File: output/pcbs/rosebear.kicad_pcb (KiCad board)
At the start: 2 copper layers, 135.3 x 105.1 mm, 43 parts

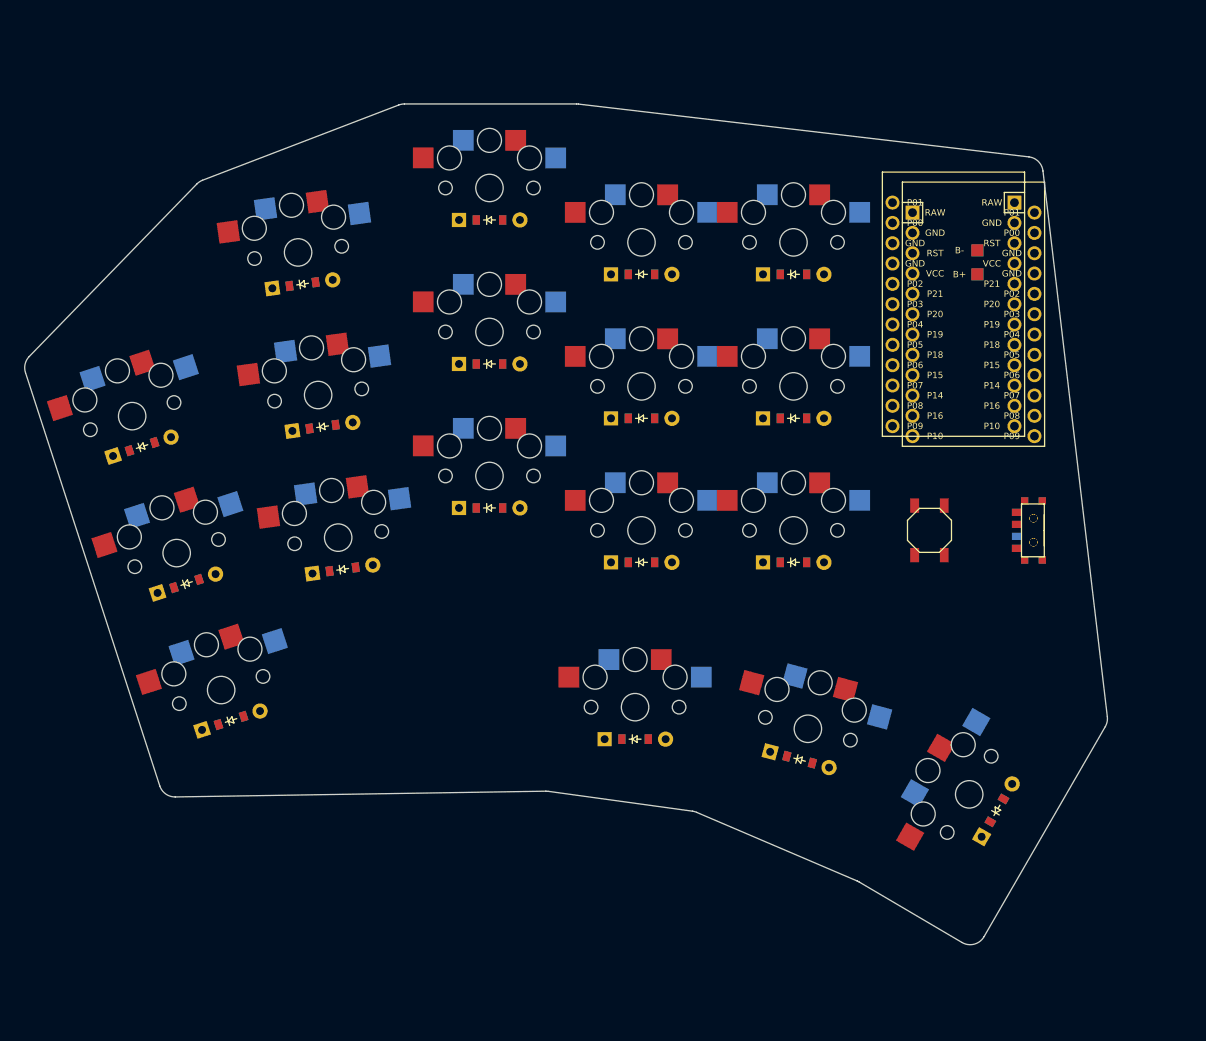
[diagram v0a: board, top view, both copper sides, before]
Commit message: inset board edge a bit
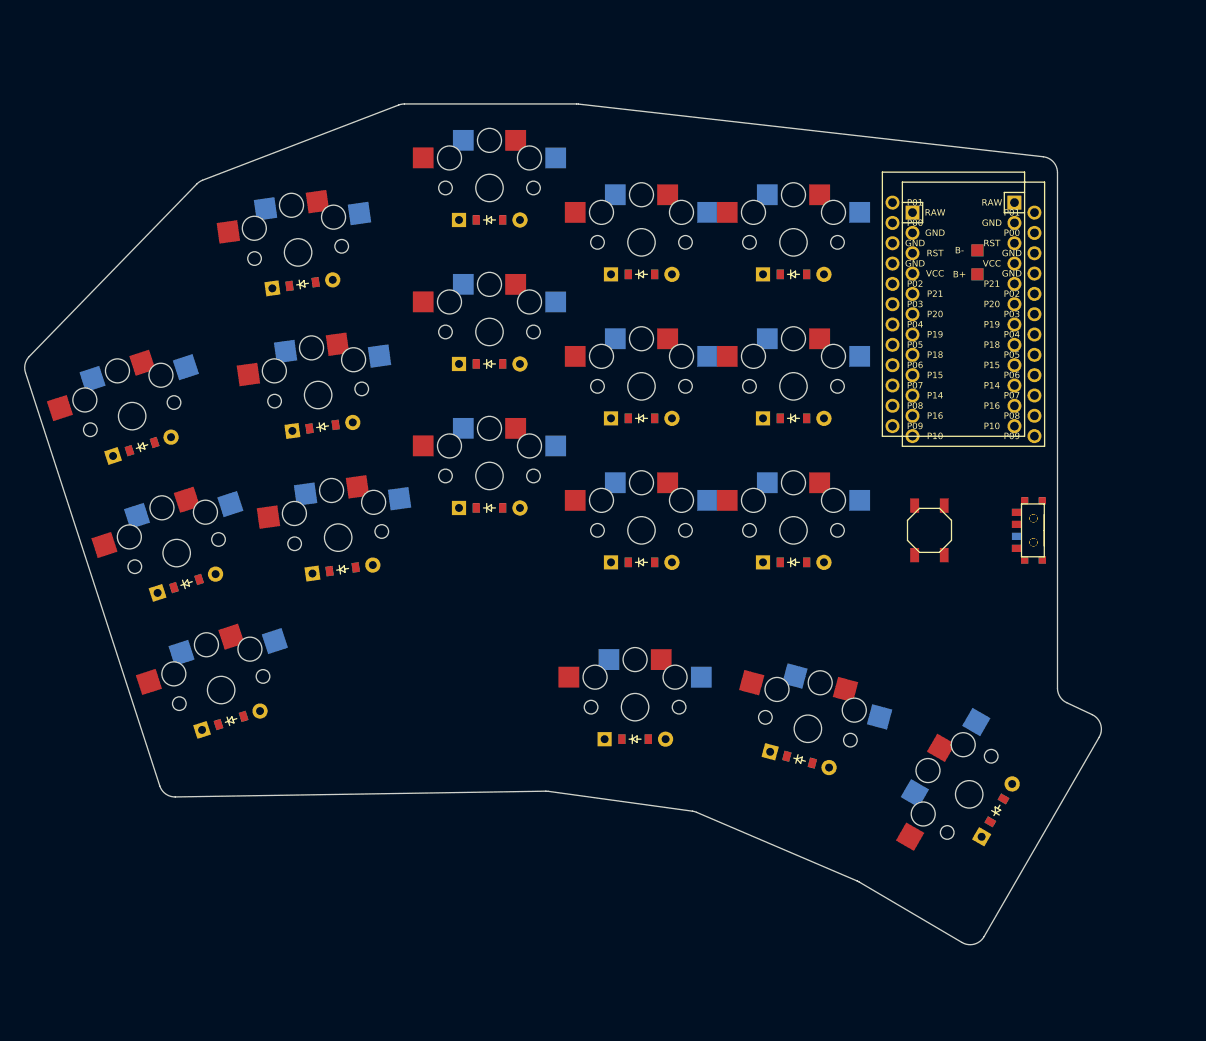
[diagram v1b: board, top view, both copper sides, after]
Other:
- board size 135.3 x 105.1 mm -> 134.6 x 105.1 mm
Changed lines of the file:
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@@
 (gr_line (start 26.00924211801839 58.31019527101077) (end 46.956701761727736 36.74665385238504) (angle 90) (layer Edge.Cuts) (width 0.15))
 (gr_line (start 47.675304323093606 36.27276563583152) (end 72.19402026968349 26.872666933425457) (angle 90) (layer Edge.Cuts) (width 0.15))
-(gr_line (start 72.90997585686867 26.740127099999995) (end 94.42288855882353 26.740127099999995) (angle 90) (layer Edge.Cuts) (width 0.15))
-(gr_line (start 94.65577615882353 26.753732499999998) (end 150.9713108649408 33.35624346554478) (angle 90) (layer Edge.Cuts) (width 0.15))
-(gr_line (start 152.72466176356932 35.10842305391452) (end 160.77044002192582 103.33990513293065) (angle 90) (layer Edge.Cuts) (width 0.15))
-(gr_line (start 160.5162523232973 104.57412014456105) (end 145.35622983220486 130.83204941203354) (angle 90) (layer Edge.Cuts) (width 0.15))
+(gr_line (start 72.90997585686867 26.740127099999995) (end 94.42675824117646 26.740127099999995) (angle 90) (layer Edge.Cuts) (width 0.15))
+(gr_line (start 94.65198304117646 26.75284909999999) (end 152.76495489999996 33.33898591066666) (angle 90) (layer Edge.Cuts) (width 0.15))
+(gr_line (start 154.53973009999999 35.32626391066666) (end 154.53973009999999 99.76916453497174) (angle 90) (layer Edge.Cuts) (width 0.15))
+(gr_line (start 155.69039535648147 101.57986341455873) (end 158.87663370340863 103.07441496462012) (angle 90) (layer Edge.Cuts) (width 0.15))
+(gr_line (start 159.75934975989009 105.88511384420713) (end 145.3562298322048 130.83204941203363) (angle 90) (layer Edge.Cuts) (width 0.15))
 (gr_line (start 142.6103300759012 131.55603033773085) (end 129.7268923040715 123.9794611751653) (angle 90) (layer Edge.Cuts) (width 0.15))
 (gr_line (start 129.49926914776796 123.86446170086256) (end 109.4288812776986 115.28369792041691) (angle 90) (layer Edge.Cuts) (width 0.15))
@@
 (gr_arc (start 48.391259910278805 38.14022580240604) (end 47.675304310278804 36.27276560240604) (angle -24.85423372436118) (layer Edge.Cuts) (width 0.15))
 (gr_arc (start 72.90997585686867 28.740127099999995) (end 72.90997585686867 26.740127099999995) (angle -20.976057573328575) (layer Edge.Cuts) (width 0.15))
-(gr_arc (start 94.42288855882353 28.740127099999995) (end 94.65577615882353 26.753732499999995) (angle -6.68690810957105) (layer Edge.Cuts) (width 0.15))
-(gr_arc (start 150.73842326494074 35.34263806554476) (end 152.72466176494075 35.10842306554476) (angle -76.58789419306477) (layer Edge.Cuts) (width 0.15))
-(gr_arc (start 158.78420152329724 103.574120144561) (end 160.51625232329724 104.574120144561) (angle -36.72519780578217) (layer Edge.Cuts) (width 0.15))
-(gr_arc (start 143.6241790322048 129.83204941203357) (end 142.6103300322048 131.55603031203356) (angle -90.45918719394365) (layer Edge.Cuts) (width 0.15))
+(gr_arc (start 94.42675824117646 28.740127099999995) (end 94.65198304117646 26.752849099999995) (angle -6.465930960313301) (layer Edge.Cuts) (width 0.15))
+(gr_arc (start 152.53973009999999 35.32626391066666) (end 154.53973009999999 35.32626391066666) (angle -83.5340690396875) (layer Edge.Cuts) (width 0.15))
+(gr_arc (start 156.53973009999999 99.76916453497174) (end 154.53973009999999 99.76916453497174) (angle -64.87038884747196) (layer Edge.Cuts) (width 0.15))
+(gr_arc (start 158.0272989598901 104.88511384420713) (end 159.75934975989009 105.88511384420713) (angle -94.87038895588762) (layer Edge.Cuts) (width 0.15))
+(gr_arc (start 143.6241790322048 129.83204941203363) (end 142.6103300322048 131.5560303120336) (angle -90.45918719394302) (layer Edge.Cuts) (width 0.15))
 (gr_arc (start 128.71304334776792 125.70344210086255) (end 129.72689234776792 123.97946120086254) (angle -7.310854726210664) (layer Edge.Cuts) (width 0.15))
 (gr_arc (start 108.64265547769858 117.1226783204169) (end 109.42888127769858 115.2836979204169) (angle -15.312815384930758) (layer Edge.Cuts) (width 0.15))

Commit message: move thumb cluster out, and other adjustments
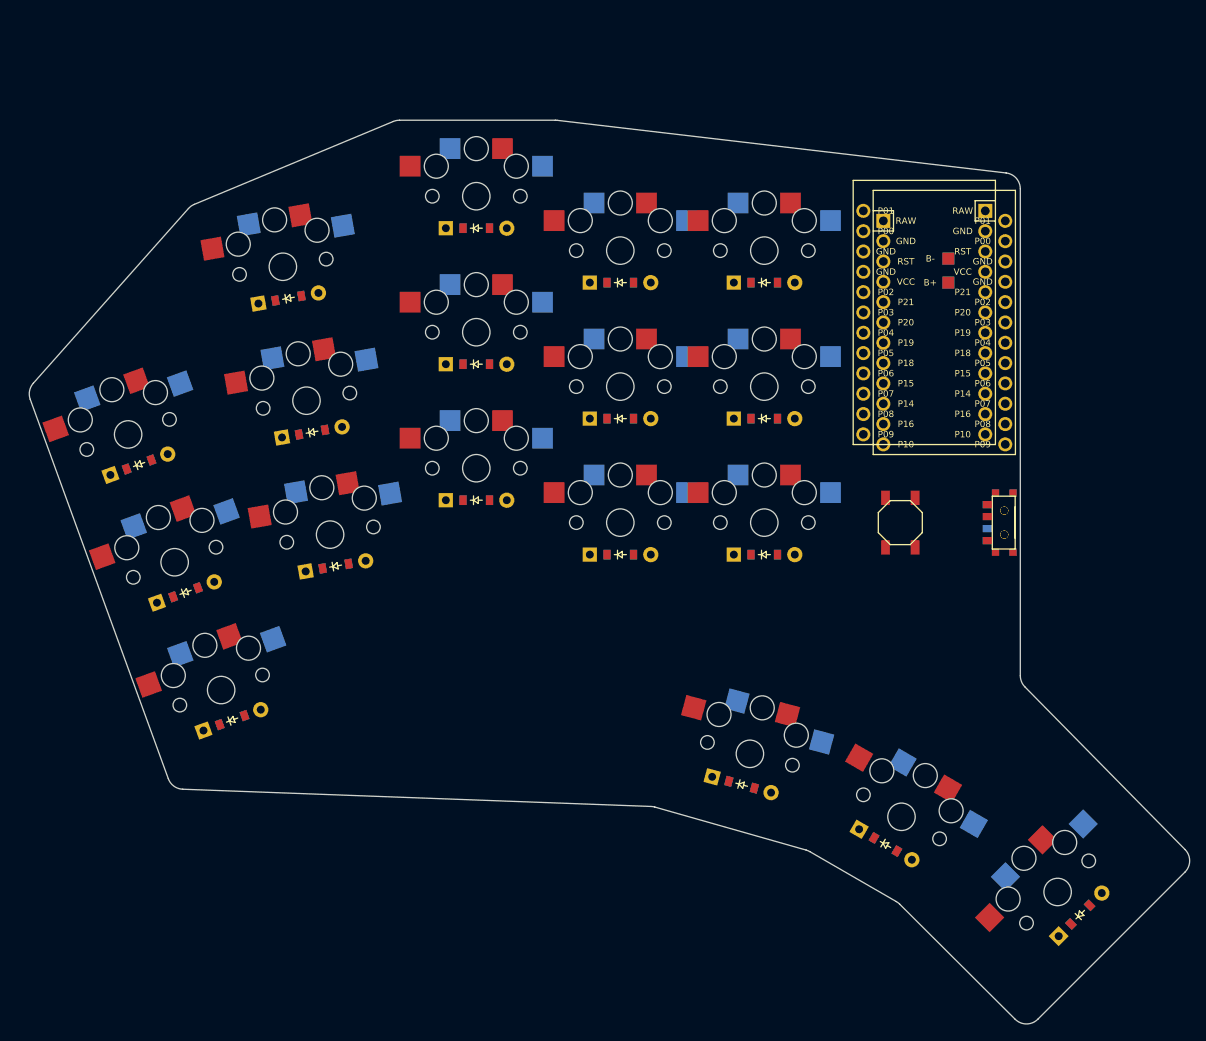
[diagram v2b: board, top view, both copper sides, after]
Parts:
- moved D18 16.7 mm to (157.4, 128.1), turned to 45 degrees
- moved S18 16.5 mm to (154.6, 125.2), turned to 45 degrees
- moved S17 16.1 mm to (135.0, 115.8), turned to -30 degrees
- moved S16 15.5 mm to (116.1, 108.0), turned to -15 degrees
- moved D17 15.1 mm to (133.0, 119.3), turned to -30 degrees
- moved D16 14.5 mm to (115.1, 111.8), turned to -15 degrees
- moved D15 3.79 mm to (117.9, 49.1)
- moved S15 3.79 mm to (117.9, 45.1)
- moved MCU1 3.79 mm to (137.9, 54.1)
- moved MCU2 3.79 mm to (140.4, 55.3)
- moved PAD1 3.79 mm to (140.9, 49.1)
- moved PAD2 3.79 mm to (140.9, 46.1)
- moved D13 3.77 mm to (117.9, 83.1)
- moved S13 3.77 mm to (117.9, 79.1)
- moved B1 3.77 mm to (134.9, 79.1)
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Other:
- board size 134.6 x 105.1 mm -> 145.1 x 113 mm

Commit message: move components around
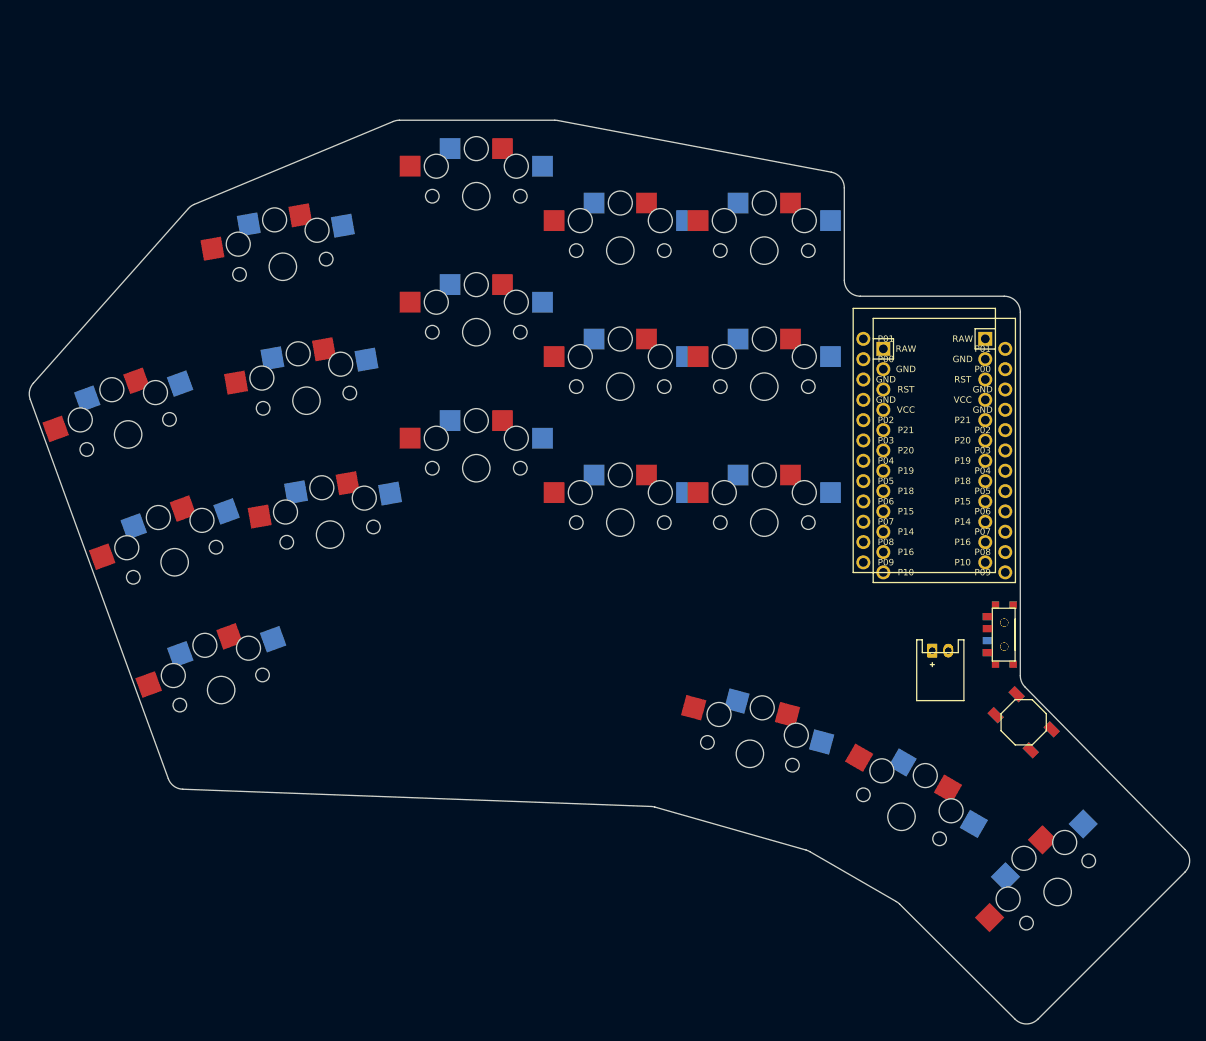
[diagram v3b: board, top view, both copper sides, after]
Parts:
- removed D1, D10, D11, D12, D13, D14, D15, D16, D17, D18, D2, D3, D4, D5, D6, D7, D8, D9: , ComboDiode
- removed PAD1, PAD2: , SMDPad
- added B2: , E73:SW_TACT_ALPS_SKQGABE010, F.Cu at (150.3, 104.0)
- added JST1, JST2: , JST_PH_S2B-PH-K_02x2.00mm_Angled, F.Cu at (139.9, 95.1)
- moved B1 29.3 mm to (150.3, 104.0), turned to 135 degrees
- moved MCU1 16.0 mm to (137.9, 70.1)
- moved MCU2 16.0 mm to (140.4, 71.3)
- moved T1 14.0 mm to (147.9, 93.1)
- moved T2 14.0 mm to (147.9, 93.1)
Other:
- outline, holes or cut-outs redrawn

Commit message: final routing
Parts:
- removed MCU2: , ProMicro
- added S19: , PG1350, F.Cu at (48.4, 87.0)
- added S20: , PG1350, F.Cu at (42.6, 71.1)
- added S21: , PG1350, F.Cu at (36.8, 55.1)
- added S22: , PG1350, F.Cu at (62.0, 67.6)
- added S23: , PG1350, F.Cu at (59.1, 50.9)
- added S24: , PG1350, F.Cu at (56.1, 34.1)
- added S25: , PG1350, F.Cu at (80.3, 59.3)
- added S26: , PG1350, F.Cu at (80.3, 42.3)
- added S27: , PG1350, F.Cu at (80.3, 25.3)
- added S28: , PG1350, F.Cu at (98.3, 66.1)
- added S29: , PG1350, F.Cu at (98.3, 49.1)
- added S30: , PG1350, F.Cu at (98.3, 32.1)
- added S31: , PG1350, F.Cu at (116.3, 66.1)
- added S32: , PG1350, F.Cu at (116.3, 49.1)
- added S33: , PG1350, F.Cu at (116.3, 32.1)
- added S34: , PG1350, F.Cu at (114.5, 95.0)
- added S35: , PG1350, F.Cu at (133.5, 102.9)
- added S36: , PG1350, F.Cu at (153.0, 112.3)
- moved S14 13.0 mm to (116.3, 49.1)
- moved S6 13.0 mm to (56.1, 34.1)
- moved T1 13.0 mm to (146.3, 80.1)
- moved T2 13.0 mm to (146.3, 80.1)
- moved S7 13.0 mm to (80.3, 59.3)
- moved S8 13.0 mm to (80.3, 42.3)
- moved S15 13.0 mm to (116.3, 32.1)
- moved S18 13.0 mm to (153.0, 112.3)
- moved S12 13.0 mm to (98.3, 32.1)
- moved S10 13.0 mm to (98.3, 66.1)
- moved S17 13.0 mm to (133.5, 102.9)
- moved S9 13.0 mm to (80.3, 25.3)
- moved S4 13.0 mm to (62.0, 67.6)
- moved JST1 13.0 mm to (138.3, 82.1)
- moved JST2 13.0 mm to (138.3, 82.1)
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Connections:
- MCU1 pad 13: P1 -> P9
- MCU1 pad 14: P0 -> P8
- MCU1 pad 15: GND -> P7
- MCU1 pad 16: GND -> P6
- MCU1 pad 17: P2 -> P5
- MCU1 pad 18: P3 -> P4
- MCU1 pad 19: P4 -> P3
- MCU1 pad 20: P5 -> P2
- MCU1 pad 21: P6 -> GND
- MCU1 pad 22: P7 -> GND
- MCU1 pad 23: P8 -> P0
- MCU1 pad 24: P9 -> P1
- S1 pad 1: P20 -> P15
- S1 pad 2: pinky_bottom -> GND
- S10 pad 1: P15 -> P20
- S10 pad 2: index_bottom -> GND
- S11 pad 1: P15 -> P6
- S11 pad 2: index_home -> GND
- S12 pad 1: P15 -> P0
- S12 pad 2: index_top -> GND
- S13 pad 1: P14 -> P21
- S13 pad 2: inner_bottom -> GND
- S14 pad 1: P14 -> P5
- S14 pad 2: inner_home -> GND
- S15 pad 1: P14 -> P1
- S15 pad 2: inner_top -> GND
- S16 pad 1: P18 -> P14
- S16 pad 2: near_thumb -> GND
- S17 pad 1: P15 -> P16
- S17 pad 2: home_thumb -> GND
- S18 pad 1: P14 -> P10
- S18 pad 2: far_thumb -> GND
- S2 pad 1: P20 -> P9
- S2 pad 2: pinky_home -> GND
- S3 pad 1: P20 -> P4
- S3 pad 2: pinky_top -> GND
- S4 pad 1: P19 -> P18
- S4 pad 2: ring_bottom -> GND
- S5 pad 1: P19 -> P8
- S5 pad 2: ring_home -> GND
- S6 pad 1: P19 -> P3
- S6 pad 2: ring_top -> GND
- S7 pad 1: P18 -> P19
- S7 pad 2: middle_bottom -> GND
- S8 pad 1: P18 -> P7
- S8 pad 2: middle_home -> GND
- S9 pad 1: P18 -> P2
- S9 pad 2: middle_top -> GND
- T1 pad 1: RAW -> Bplus
- T1 pad 2: Bplus -> RAW
- T2 pad 1: RAW -> Bplus
- T2 pad 2: Bplus -> RAW
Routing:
- net GND: track 0.00 -> 960.7 mm
- net P4: track 0.00 -> 164.3 mm
- net P9: track 0.00 -> 155.9 mm
- net P15: track 0.00 -> 132.7 mm
- net P3: track 0.00 -> 129.1 mm
- net P8: track 0.00 -> 121.9 mm
- net P18: track 0.00 -> 114.0 mm
- net P2: track 0.00 -> 101.3 mm
- net P19: track 0.00 -> 100.8 mm
- net P7: track 0.00 -> 97.2 mm
- net RAW: track 0.00 -> 95.3 mm
- net P10: track 0.00 -> 82.4 mm
- net P20: track 0.00 -> 79.8 mm
- net P16: track 0.00 -> 75.0 mm
- net P6: track 0.00 -> 73.9 mm
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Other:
- net class Default removed
- rule pad_to_mask_clearance: 0.05 -> 0
- board text added: "ROSEBEAR. "
